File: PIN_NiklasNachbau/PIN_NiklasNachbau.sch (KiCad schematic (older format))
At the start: 20 parts

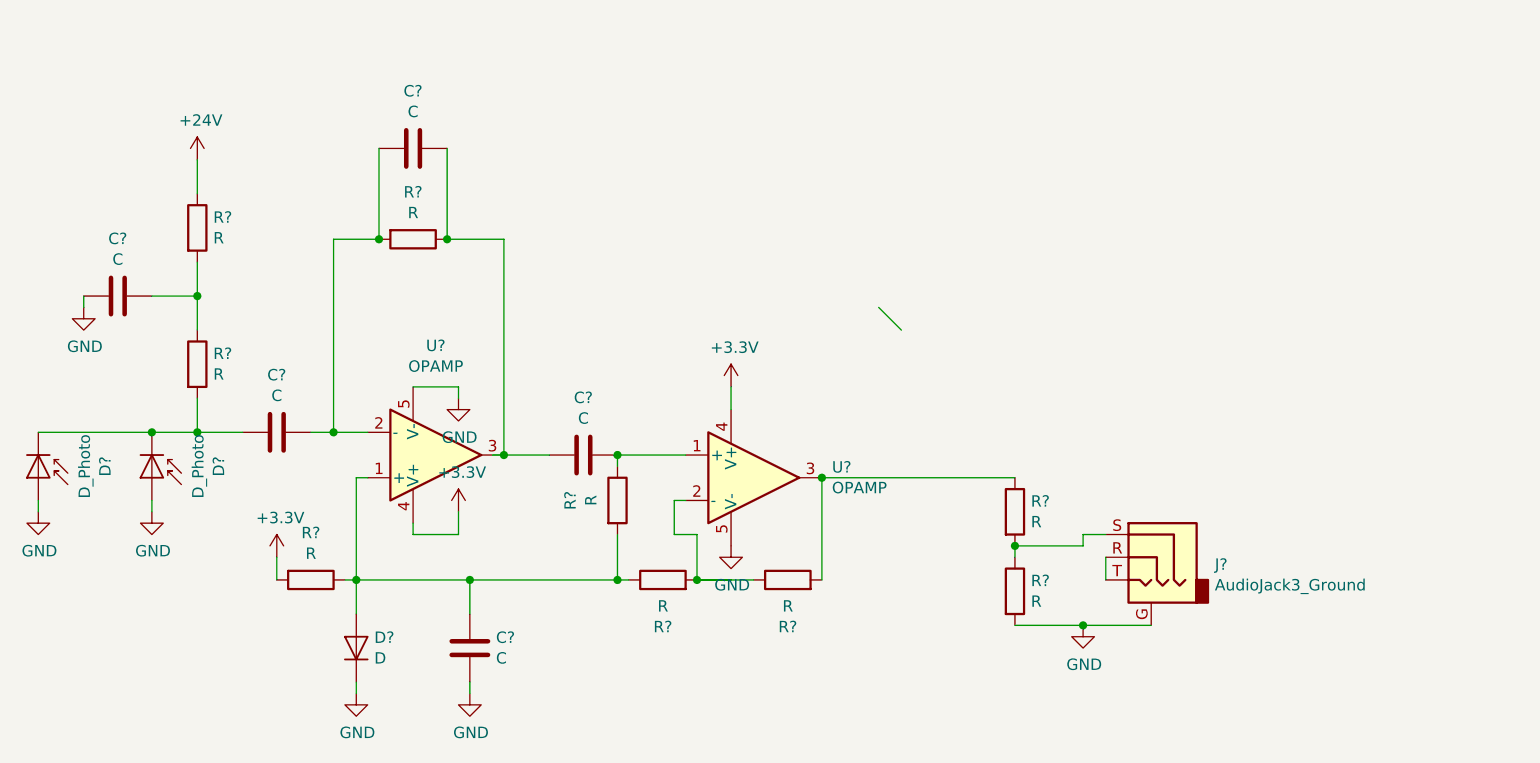
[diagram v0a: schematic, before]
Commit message: designed proof of concept pcb
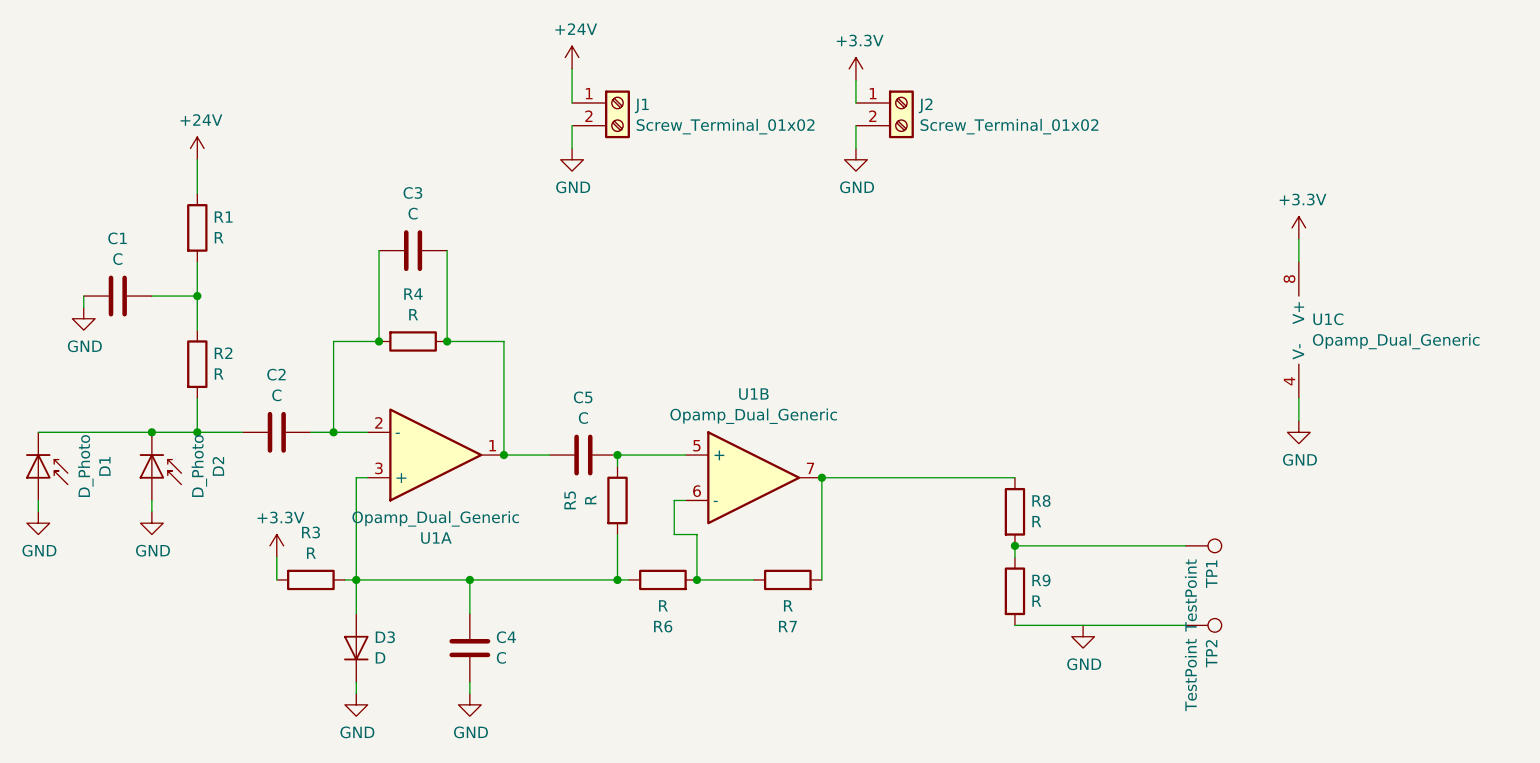
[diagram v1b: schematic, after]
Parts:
- removed J?: AudioJack3_Ground, symbol Connector:AudioJack3_Ground
- removed U? (x2): OPAMP, symbol pspice:OPAMP
- added J1, J2: Screw_Terminal_01x02, TerminalBlock:TerminalBlock_bornier-2_P5.08mm, symbol Connector:Screw_Terminal_01x02
- added TP1, TP2: TestPoint, TestPoint:TestPoint_Pad_4.0x4.0mm, symbol Connector:TestPoint
- added U1: Opamp_Dual_Generic, Package_SO:SOIC-8_5.23x5.23mm_P1.27mm, symbol Device:Opamp_Dual_Generic
- C1, C2, C3, C4, C5: renamed from C?; footprint (none) -> Capacitor_SMD:C_0805_2012Metric_Pad1.15x1.40mm_HandSolder
- D1, D2: renamed from D?; footprint (none) -> OptoDevice:Osram_DIL2_4.3x4.65mm_P5.08mm
- D3: renamed from D?; footprint (none) -> Diode_THT:D_DO-35_SOD27_P7.62mm_Horizontal
- R1, R7: renamed from R?; footprint (none) -> Resistor_SMD:R_1206_3216Metric_Pad1.42x1.75mm_HandSolder
- R2, R3, R4, R5, R6, R8, R9: renamed from R?; footprint (none) -> Resistor_SMD:R_0805_2012Metric_Pad1.15x1.40mm_HandSolder
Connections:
- wire segments 56 -> 51
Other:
- moved on the sheet: C3, R4
